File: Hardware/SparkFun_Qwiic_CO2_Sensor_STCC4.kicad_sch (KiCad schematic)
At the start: 27 parts, among them J1 Qwiic_RA, J2 Qwiic_RA, J3 Conn_01x06, U2 STCC4, U3 SHT40

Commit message: Updated to v10 for REDs
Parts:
- U2: PROD_ID IC-... -> IC-28635
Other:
- note added: "Cut jumper to remove I2C pullups"

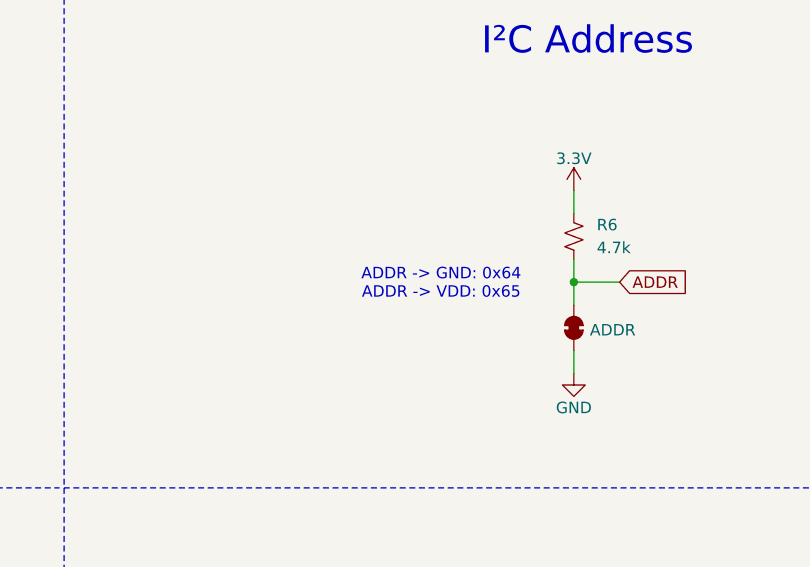
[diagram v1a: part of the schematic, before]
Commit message: Updated I2C Address
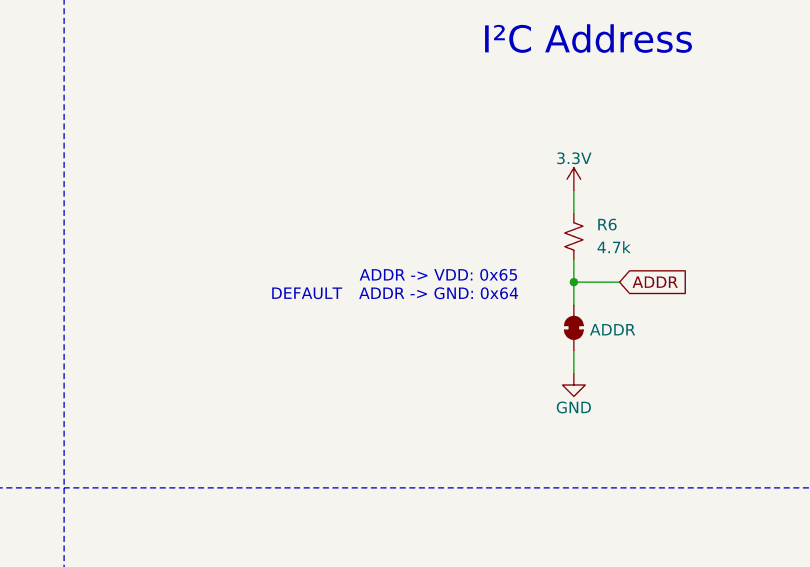
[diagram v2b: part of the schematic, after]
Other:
- note added: "ADDR -> VDD: 0x65 ADDR -> GND: 0x64"
- note added: "DEFAULT"
- note removed: "ADDR -> GND: 0x64 ADDR -> VDD: 0x65"
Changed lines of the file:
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@@
 		)
 	)
-	(text "ADDR -> GND: 0x64\nADDR -> VDD: 0x65\n"
+	(text "ADDR -> VDD: 0x65\nADDR -> GND: 0x64"
 		(exclude_from_sim no)
-		(at 198.628 120.904 0)
+		(at 198.374 121.158 0)
 		(effects
 			(font
@@
 			)
 		)
+	)
+	(text "DEFAULT"
+		(exclude_from_sim no)
+		(at 183.642 122.174 0)
+		(effects
+			(font
+				(size 1.27 1.27)
+				(color 132 132 132 1)
+			)
+		)
